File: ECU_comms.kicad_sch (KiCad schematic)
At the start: 10 parts, among them U1 TJA1051TK-3, U10 NTS0104GU12_115, U3 TSS463C, U8 ABM3B-8.000MHZ-B2-T

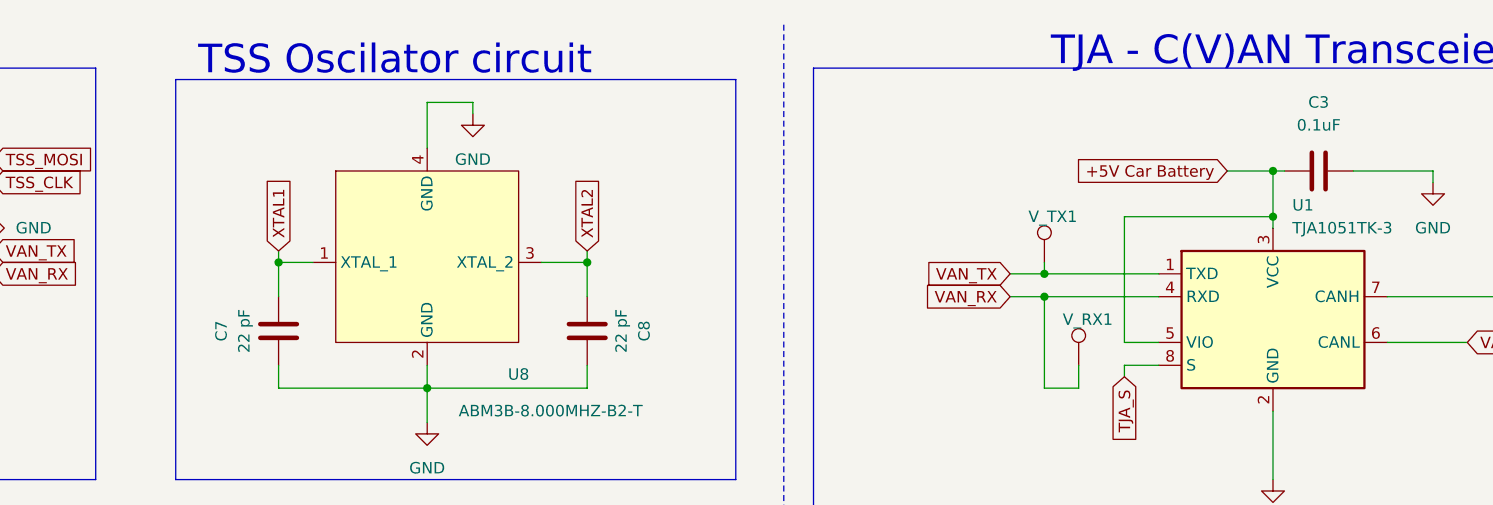
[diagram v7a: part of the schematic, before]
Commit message: Change inductor type.
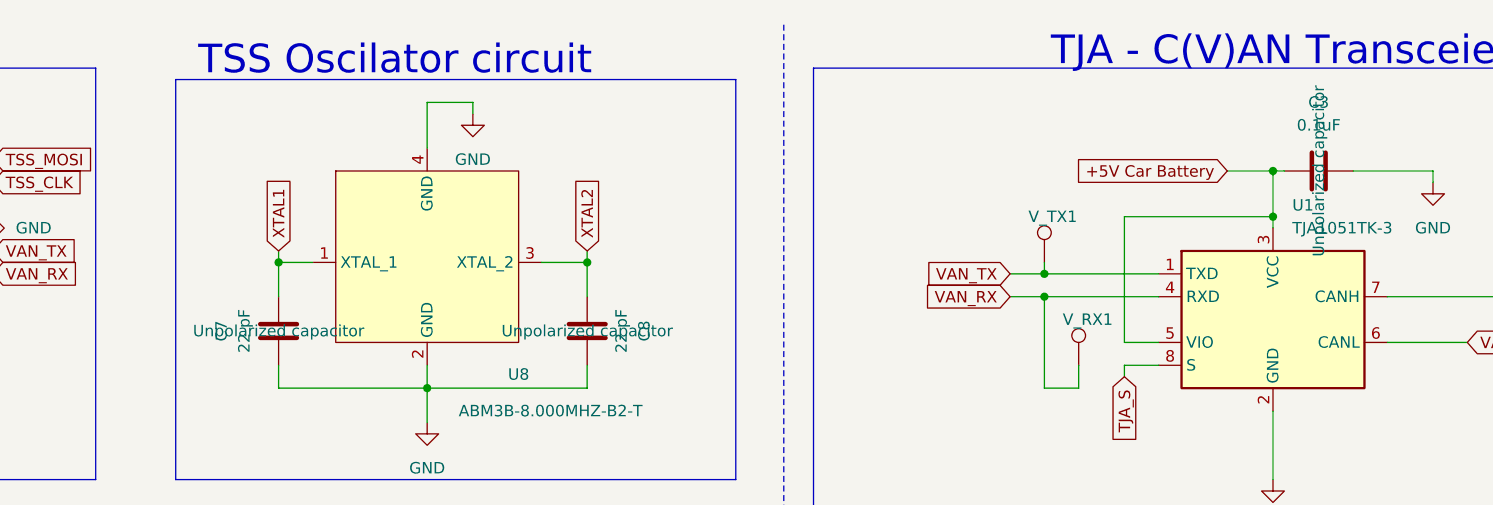
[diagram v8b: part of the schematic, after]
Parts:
- U3: footprint intoftainment:TSS463C -> lib:TSS463C
- U8: footprint Crystal:Crystal_SMD_EuroQuartz_MJ-4Pin_5.0x3.2mm -> Crystal:Crystal_SMD_Abracon_ABM3B-4Pin_5.0x3.2mm
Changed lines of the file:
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@@
 			)
 		)
-		(property "Description" ""
+		(property "Description" "Unpolarized capacitor"
 			(at 229.87 30.48 0)
 			(effects
@@
 			)
 		)
-		(property "Footprint" "intoftainment:TSS463C"
+		(property "Footprint" "lib:TSS463C"
 			(at 63.5 39.37 0)
 			(effects
@@
 			)
 		)
-		(property "Footprint" "Crystal:Crystal_SMD_EuroQuartz_MJ-4Pin_5.0x3.2mm"
+		(property "Footprint" "Crystal:Crystal_SMD_Abracon_ABM3B-4Pin_5.0x3.2mm"
 			(at 140.97 55.88 0)
 			(effects
@@
 			)
 		)
-		(property "Description" ""
+		(property "Description" "Unpolarized capacitor"
 			(at 114.3 48.26 0)
 			(effects
@@
 			)
 		)
-		(property "Description" ""
+		(property "Description" "Unpolarized capacitor"
 			(at 148.59 48.26 0)
 			(effects
